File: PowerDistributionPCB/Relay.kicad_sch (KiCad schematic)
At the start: 0 parts

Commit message: fixed relay
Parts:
- added D2: 1N4007, Diode_THT:D_DO-41_SOD81_P10.16mm_Horizontal, symbol Diode:1N4007
- added K1: Relay, ORWH-SH-105D1F_000:RELAY_ORWH-SH-105D1F_000, symbol Relays:ORWH-SH-105D1F_000
- added Q1: PN2222A, Package_TO_SOT_THT:TO-92_Inline, symbol Transistor_BJT:PN2222A
- added R3: R, symbol Device:R
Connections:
- new net: Q1.2 (B), R3.2
- new net: D2.2 (A), K1.5, Q1.3 (C)
- new net 5V: D2.1 (K), K1.3
- new net ArduinoConnection: R3.1
- new net GND: Q1.1 (E)
- new net Out: K1.2
- new net VIN: K1.4

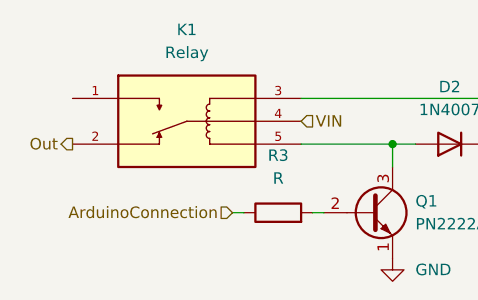
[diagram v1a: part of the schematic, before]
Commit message: cleaned up main, updated labels
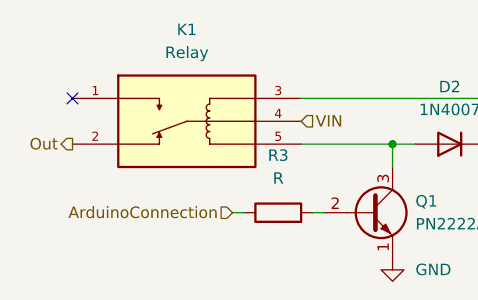
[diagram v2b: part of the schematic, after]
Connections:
- no-connect marks 0 -> 1
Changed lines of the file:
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@@
 		(color 0 0 0 0)
+	)
+	(no_connect
+		(at 111.76 69.85)
 	)
 	(wire

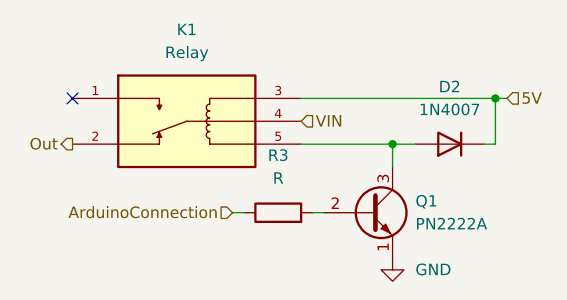
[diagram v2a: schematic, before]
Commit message: updates to layout and connectors
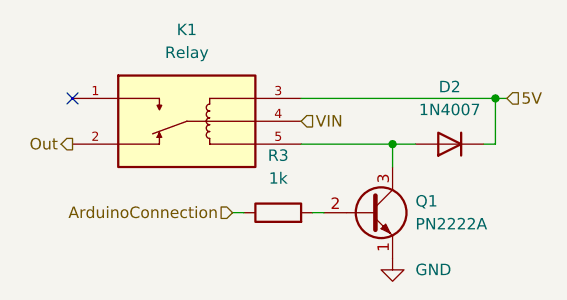
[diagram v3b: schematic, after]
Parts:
- R3: value R -> 1k
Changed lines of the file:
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@@
 			)
 		)
-		(property "Value" "R"
+		(property "Value" "1k"
 			(at 134.62 78.74 90)
 			(effects

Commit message: new relays
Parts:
- added D10, D6: 1N4148, Diode_THT:D_DO-35_SOD27_P7.62mm_Horizontal, symbol Diode:1N4148
- added K2: RT314F05(gen), TE_8-1393239-5, symbol CU_Sail:RT314F05(gen)
- added Q2, Q6: MMBT2222A, Package_TO_SOT_SMD:SOT-23, symbol Transistor_BJT:MMBT2222A
- added R11, R7: 1k, symbol Device:R
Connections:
- net 5V: now also D10.1 (K), D6.1 (K), K2.A3
- net GND: now also Q2.2 (E), Q6.2 (E)
- net Out: now also K2.14.1
- net VIN: now also K2.11.1
- new net: D10.2 (A), K2.A1, Q6.3 (C)
- new net: D6.2 (A), K2.A2, Q2.3 (C)
- new net: Q2.1 (B), R11.2
- new net: Q6.1 (B), R7.2
- new net ArduinoOFF: R11.1
- new net ArduinoON: R7.1
- no-connect marks 1 -> 5
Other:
- moved on the sheet: D2, K1, Q1, R3

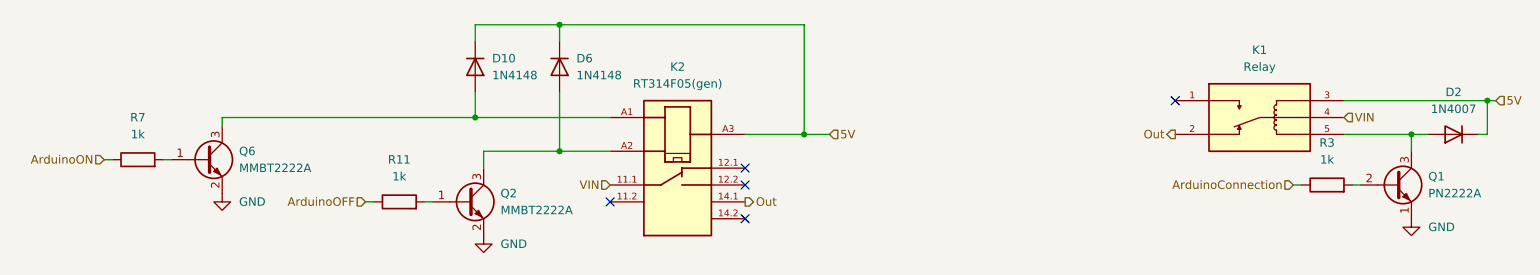
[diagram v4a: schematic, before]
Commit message: finished new relay implementation
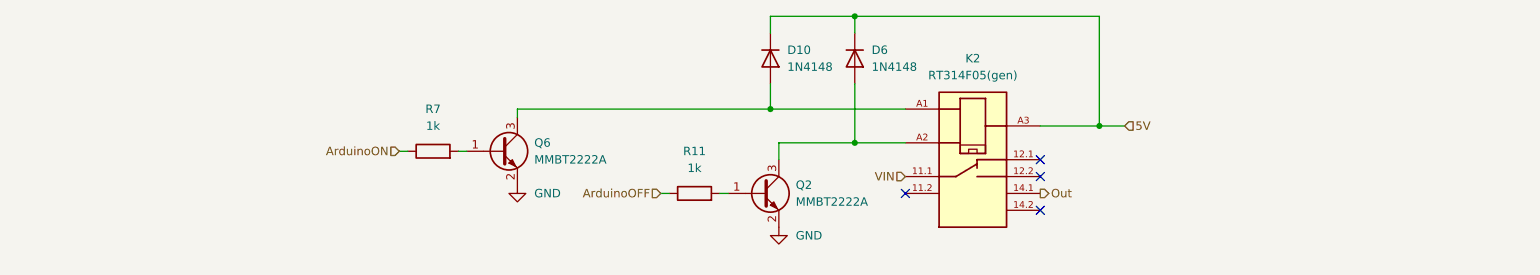
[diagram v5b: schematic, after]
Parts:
- removed D2: 1N4007, Diode_THT:D_DO-41_SOD81_P10.16mm_Horizontal, symbol Diode:1N4007
- removed K1: Relay, ORWH-SH-105D1F_000:RELAY_ORWH-SH-105D1F_000, symbol Relays:ORWH-SH-105D1F_000
- removed Q1: PN2222A, Package_TO_SOT_THT:TO-92_Inline, symbol Transistor_BJT:PN2222A
- removed R3: 1k, symbol Device:R
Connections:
- no-connect marks 5 -> 4
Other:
- moved on the sheet: D10, D6, K2, Q2, Q6, R11, R7

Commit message: more footprints on power board
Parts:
- R11, R7: footprint (none) -> Resistor_SMD:R_0805_2012Metric_Pad1.20x1.40mm_HandSolder
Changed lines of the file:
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@@
 			)
 		)
-		(property "Footprint" ""
+		(property "Footprint" "Resistor_SMD:R_0805_2012Metric_Pad1.20x1.40mm_HandSolder"
 			(at 91.44 75.438 90)
 			(effects
@@
 			)
 		)
-		(property "Footprint" ""
+		(property "Footprint" "Resistor_SMD:R_0805_2012Metric_Pad1.20x1.40mm_HandSolder"
 			(at 130.81 81.788 90)
 			(effects

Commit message: assigned custom footprints
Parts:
- K2: footprint TE_8-1393239-5 -> CUSail:RT314F05
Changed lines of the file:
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@@
 			)
 		)
-		(property "Footprint" "TE_8-1393239-5"
+		(property "Footprint" "CUSail:RT314F05"
 			(at 172.72 72.39 0)
 			(effects

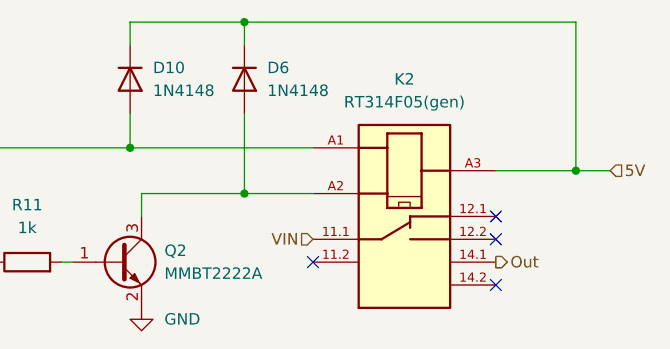
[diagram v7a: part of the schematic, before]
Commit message: update layout, adjust relay connections/footprint
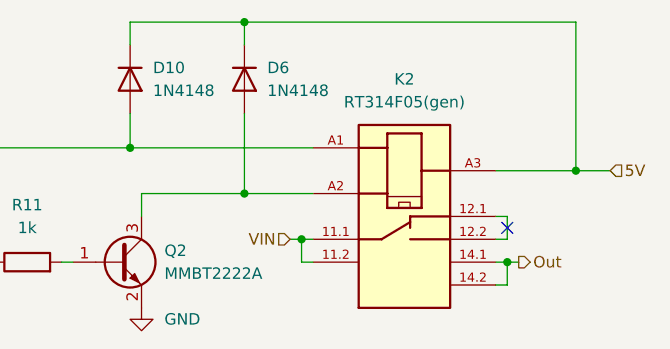
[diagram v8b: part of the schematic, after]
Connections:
- net Out: now also K2.14.2
- net VIN: now also K2.11.2
- net at K2.12.1: now also K2.12.2
- no-connect marks 4 -> 1
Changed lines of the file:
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@@
+	)
+	(junction
+		(at 184.15 80.01)
+		(diameter 0)
+		(color 0 0 0 0)
 	)
 	(junction
@@
 	)
 	(junction
+		(at 161.29 77.47)
+		(diameter 0)
+		(color 0 0 0 0)
+	)
+	(junction
 		(at 154.94 53.34)
 		(diameter 0)
@@
 	)
 	(no_connect
-		(at 182.88 74.93)
-	)
-	(no_connect
-		(at 162.56 80.01)
-	)
-	(no_connect
-		(at 182.88 82.55)
-	)
-	(no_connect
-		(at 182.88 77.47)
+		(at 184.15 76.2)
+	)
+	(wire
+		(pts
+			(xy 161.29 77.47) (xy 162.56 77.47)
+		)
+		(stroke
+			(width 0)
+			(type default)
+		)
 	)
 	(wire
@@
 	(wire
 		(pts
+			(xy 162.56 80.01) (xy 161.29 80.01)
+		)
+		(stroke
+			(width 0)
+			(type default)
+		)
+	)
+	(wire
+		(pts
+			(xy 184.15 77.47) (xy 184.15 74.93)
+		)
+		(stroke
+			(width 0)
+			(type default)
+		)
+	)
+	(wire
+		(pts
 			(xy 195.58 69.85) (xy 191.77 69.85)
 		)
@@
 	(wire
 		(pts
+			(xy 182.88 82.55) (xy 184.15 82.55)
+		)
+		(stroke
+			(width 0)
+			(type default)
+		)
+	)
+	(wire
+		(pts
+			(xy 184.15 80.01) (xy 182.88 80.01)
+		)
+		(stroke
+			(width 0)
+			(type default)
+		)
+	)
+	(wire
+		(pts
+			(xy 182.88 77.47) (xy 184.15 77.47)
+		)
+		(stroke
+			(width 0)
+			(type default)
+		)
+	)
+	(wire
+		(pts
 			(xy 95.25 73.66) (xy 96.52 73.66)
 		)
@@
 	(wire
 		(pts
+			(xy 184.15 74.93) (xy 182.88 74.93)
+		)
+		(stroke
+			(width 0)
+			(type default)
+		)
+	)
+	(wire
+		(pts
 			(xy 154.94 72.39) (xy 143.51 72.39)
 		)
@@
 	(wire
 		(pts
+			(xy 161.29 80.01) (xy 161.29 77.47)
+		)
+		(stroke
+			(width 0)
+			(type default)
+		)
+	)
+	(wire
+		(pts
+			(xy 184.15 82.55) (xy 184.15 80.01)
+		)
+		(stroke
+			(width 0)
+			(type default)
+		)
+	)
+	(wire
+		(pts
+			(xy 160.02 77.47) (xy 161.29 77.47)
+		)
+		(stroke
+			(width 0)
+			(type default)
+		)
+	)
+	(wire
+		(pts
 			(xy 143.51 72.39) (xy 143.51 74.93)
 		)
@@
 		(pts
 			(xy 104.14 67.31) (xy 104.14 68.58)
+		)
+		(stroke
+			(width 0)
+			(type default)
+		)
+	)
+	(wire
+		(pts
+			(xy 185.42 80.01) (xy 184.15 80.01)
 		)
 		(stroke
@@
 	(hierarchical_label "Out"
 		(shape output)
-		(at 182.88 80.01 0)
+		(at 185.42 80.01 0)
 		(effects
 			(font
@@
 	(hierarchical_label "VIN"
 		(shape input)
-		(at 162.56 77.47 180)
+		(at 160.02 77.47 180)
 		(effects
 			(font
